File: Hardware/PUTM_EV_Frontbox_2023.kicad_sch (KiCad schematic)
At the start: 25 parts, among them J1 Conn_02x16_Counter_Clockwise, J3 M80-5100622, J4 M80-5100622, U1 LM4040C33FTA, U2 STM32G473RCTx

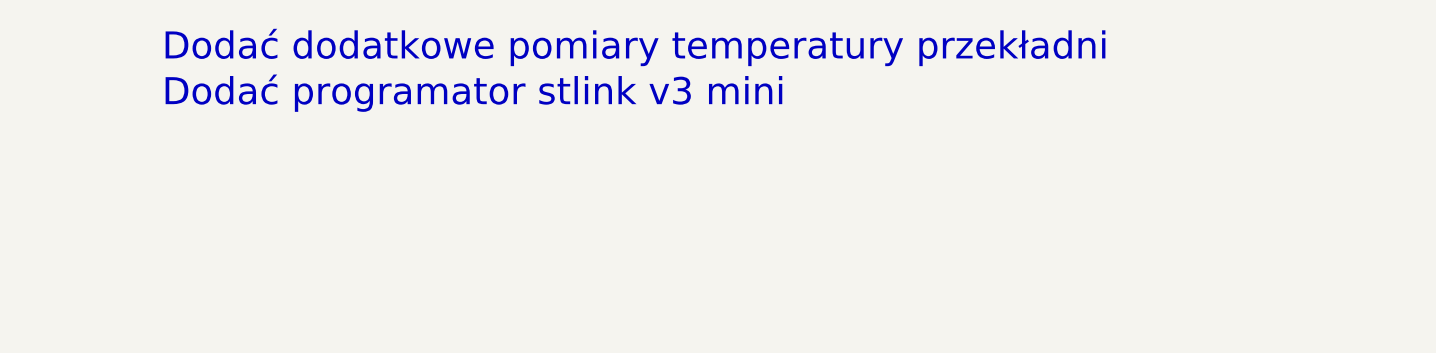
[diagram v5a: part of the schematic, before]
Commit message: Changes in converter layout and tensometers schematic
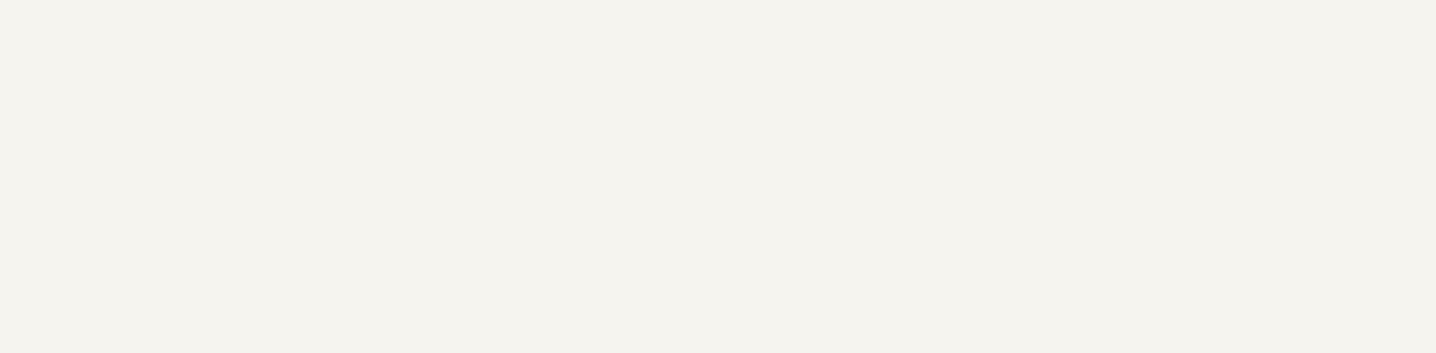
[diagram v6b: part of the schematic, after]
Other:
- note removed: "Dodać dodatkowe pomiary temperatury przekładni"
- note removed: "Dodać programator stlink v3 mini"
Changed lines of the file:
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@@
-		)
-	)
-	(text "Dodać programator stlink v3 mini\n"
-		(exclude_from_sim no)
-		(at 312.166 -6.858 0)
-		(effects
-			(font
-				(size 3 3)
-			)
-			(justify left bottom)
 		)
 	)
@@
 			)
 			(justify left bottom)
-		)
-	)
-	(text "Dodać dodatkowe pomiary temperatury przekładni"
-		(exclude_from_sim no)
-		(at 312.166 -11.938 0)
-		(effects
-			(font
-				(size 3 3)
-			)
-			(justify left bottom)
